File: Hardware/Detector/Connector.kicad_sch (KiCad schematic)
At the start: 3 parts

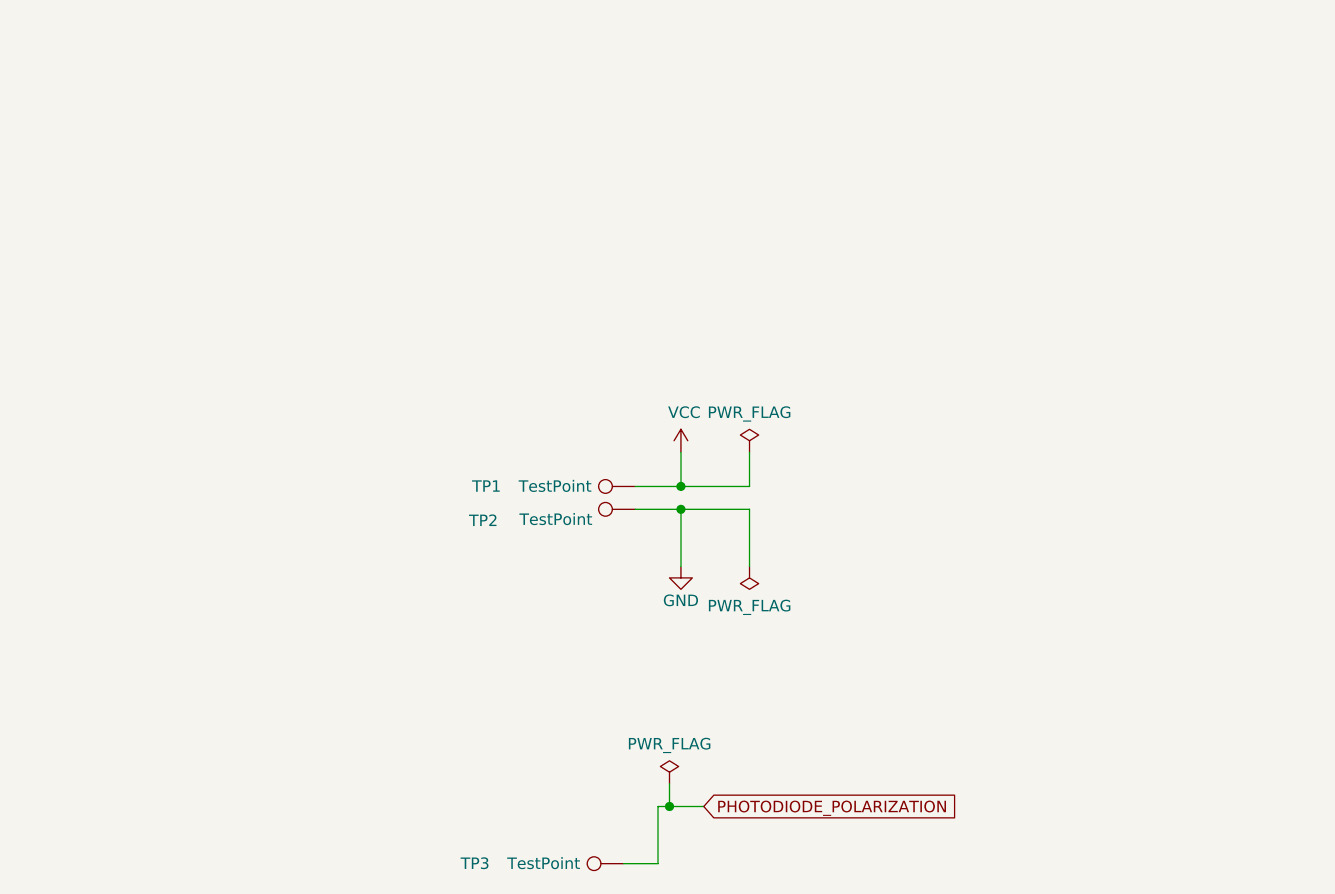
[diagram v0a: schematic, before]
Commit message: fixed footprints, changed kicad scheet name, added a bit of decription to schematics
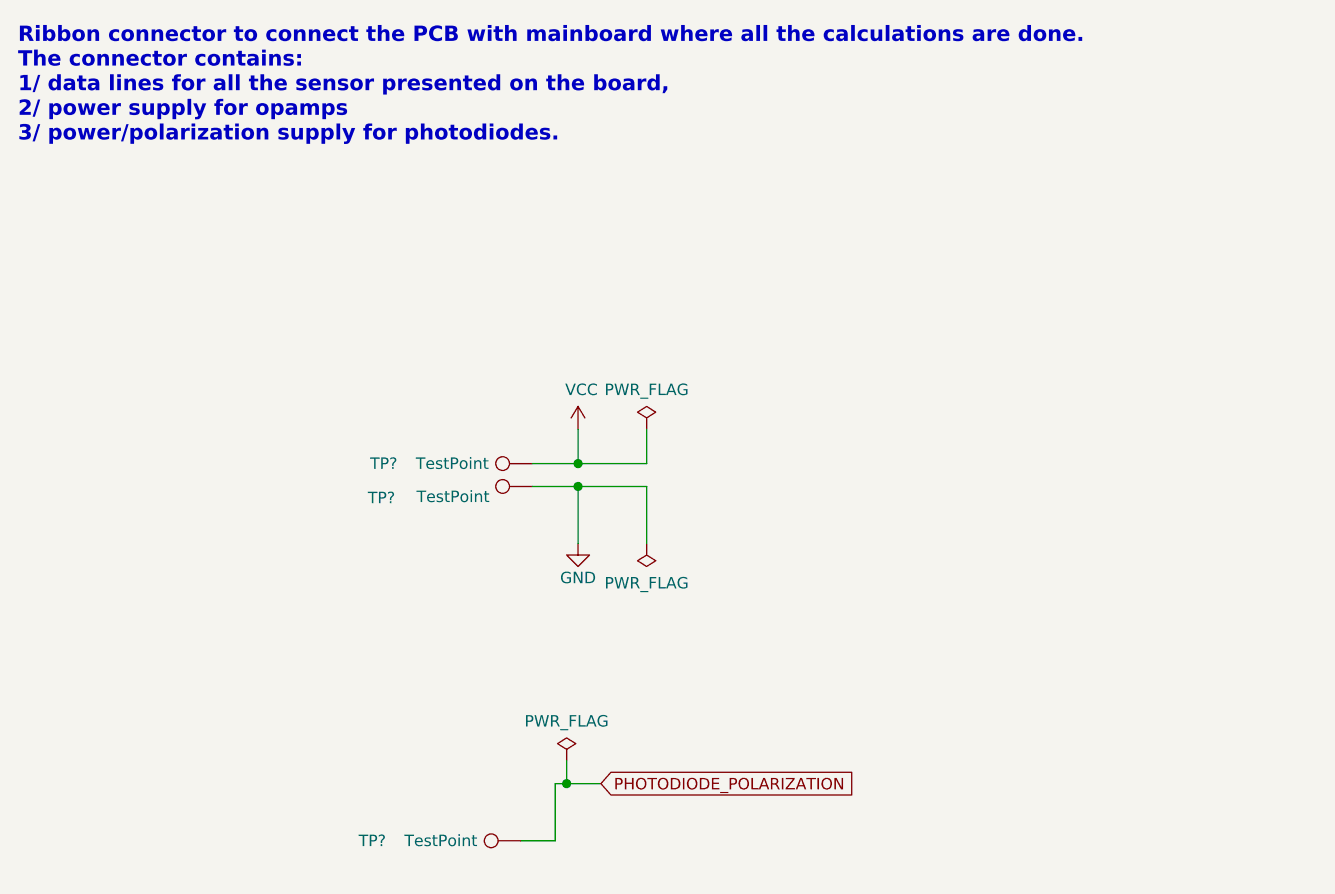
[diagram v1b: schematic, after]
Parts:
- removed TP1, TP2, TP3: TestPoint, TestPoint:TestPoint_THTPad_D2.5mm_Drill1.2mm, symbol Connector:TestPoint
- added TP? (x3): TestPoint, TestPoint:TestPoint_THTPad_D2.5mm_Drill1.2mm, symbol Connector:TestPoint
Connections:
- net GND: now also TP?.1
- net PHOTODIODE_POLARIZATION: now also TP?.1
- net VCC: now also TP?.1
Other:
- note added: "Ribbon connector to connect the PCB with mainboard where all the calculations are done. The connector contains: 1/ data lines for all the sensor presented on the board, 2/ power supply for opamps 3/ power/polarization supply for photodiodes."
- company: (none) -> Ribbon cable connector.
